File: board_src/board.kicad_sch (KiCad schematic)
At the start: 40 parts, among them J1 Conn_01x05, J16 Conn_01x05, J17 Conn_01x05, J18 Conn_02x20_Counter_Clockwise, J2 Conn_01x05, J20 Conn_02x20_Counter_Clockwise, J21 Conn_02x20_Counter_Clockwise, J22 Conn_02x20_Counter_Clockwise, J26 Conn_01x20_Socket, J27 Conn_01x20_Socket, J30 Conn_01x05, J31 Conn_01x05, J36 Conn_01x20_Socket, J37 Conn_01x20_Socket, J40 Conn_01x01_Pin, J41 Conn_01x01_Pin, J42 Conn_01x01_Pin, J43 Conn_01x01_Pin, J44 Conn_01x01_Pin, J46 Conn_01x01_Pin

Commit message: najnowsza wersja
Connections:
- no-connect marks 8 -> 2
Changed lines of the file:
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@@
-	)
-	(no_connect
-		(at 67.31 72.39)
-	)
-	(no_connect
-		(at 209.55 74.93)
-	)
-	(no_connect
-		(at 207.01 74.93)
 	)
 	(no_connect
@@
 	)
 	(no_connect
-		(at 69.85 72.39)
-	)
-	(no_connect
-		(at 204.47 74.93)
-	)
-	(no_connect
-		(at 64.77 72.39)
-	)
-	(no_connect

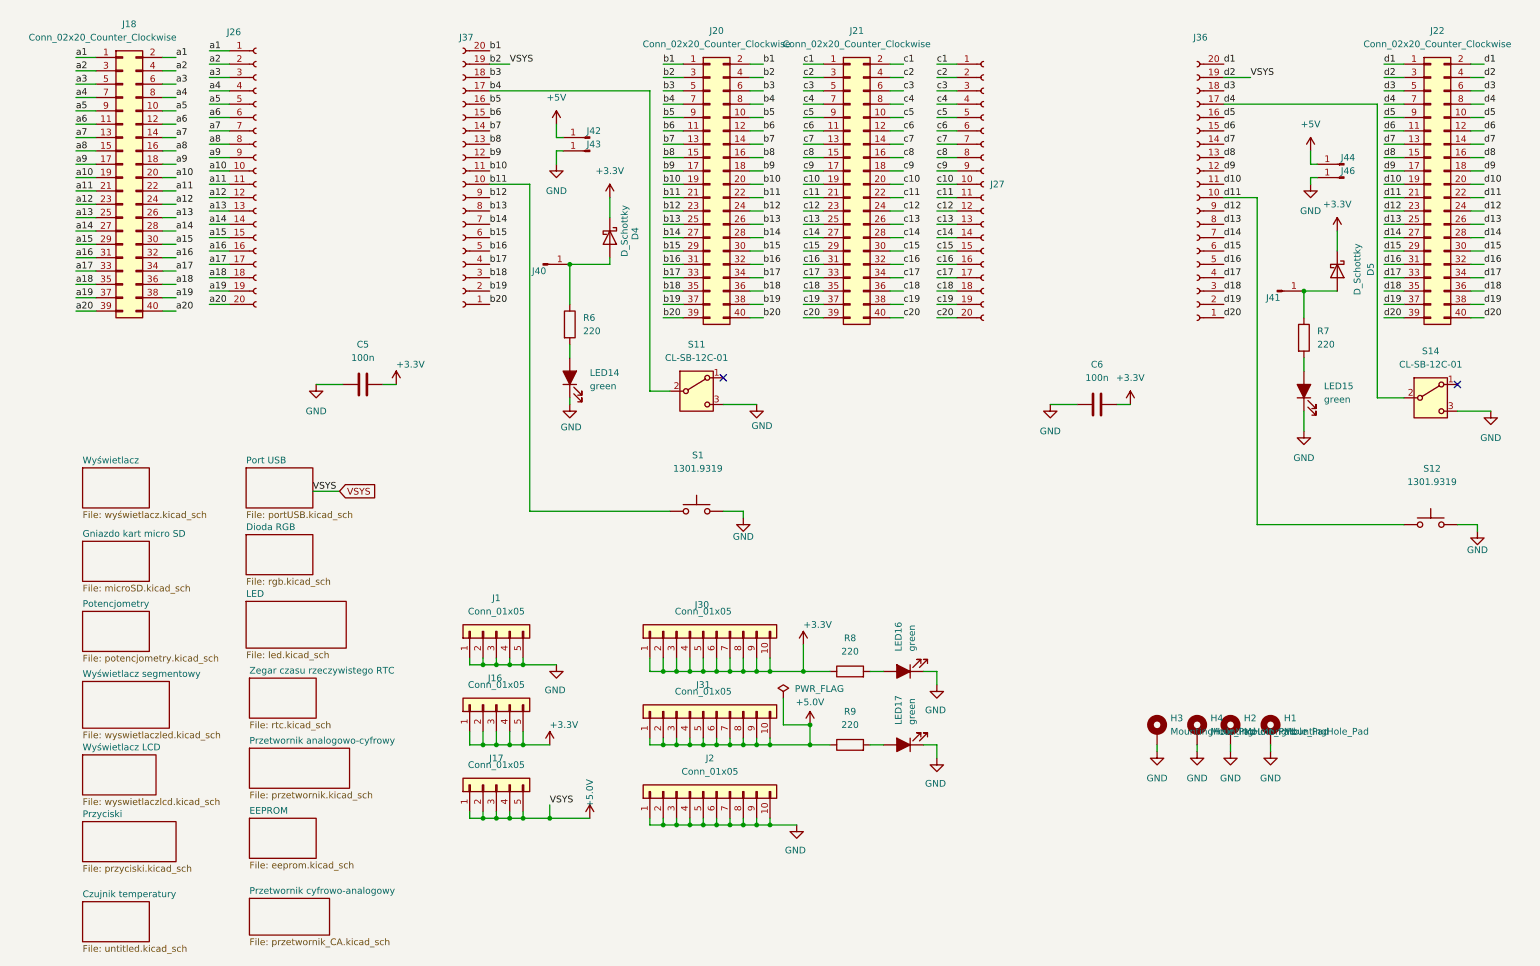
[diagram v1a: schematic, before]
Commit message: Poprawki w schematach. Rozpoczęte korekty płytki
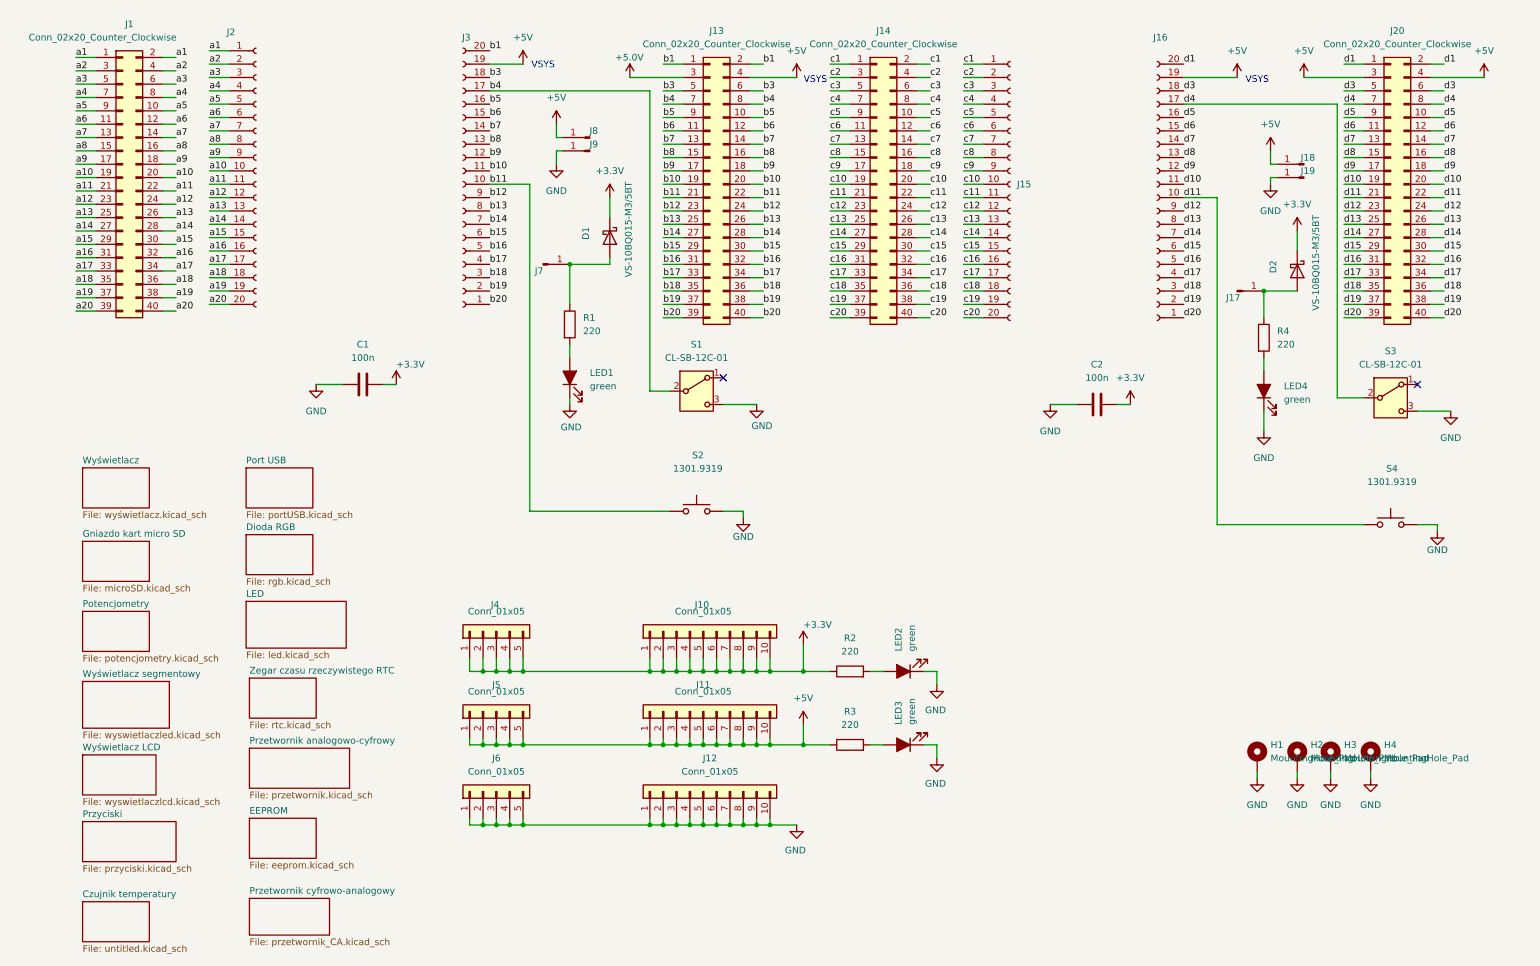
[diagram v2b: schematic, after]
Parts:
- removed D4, D5: D_Schottky, Diode_SMD:D_SMA, symbol Device:D_Schottky
- added D1, D2: VS-10BQ015-M3/5BT, Diode_SMD:D_SMB_Handsoldering, symbol Device:D_Schottky
- C1: renamed from C5; footprint Capacitor_SMD:C_0603_1608Metric -> Capacitor_SMD:C_0603_1608Metric_Pad1.08x0.95mm_HandSolder
- C2: renamed from C6; footprint Capacitor_SMD:C_0603_1608Metric -> Capacitor_SMD:C_0603_1608Metric_Pad1.08x0.95mm_HandSolder
- J1: renamed from J18; footprint Connector_PinHeader_2.54mm:PinHeader_2x20_P2.54mm_Vertical -> Connector_PinHeader_2.54mm:PinHeader_1x05_P2.54mm_Vertical
- J10: renamed from J30; footprint Connector_PinHeader_2.54mm:PinHeader_1x10_P2.54mm_Vertical -> Connector_PinHeader_2.54mm:PinHeader_2x02_P2.54mm_Vertical
- J11: renamed from J31; footprint Connector_PinHeader_2.54mm:PinHeader_1x10_P2.54mm_Vertical -> Connector_PinHeader_2.54mm:PinHeader_1x03_P2.54mm_Vertical
- J12: renamed from J2; footprint Connector_PinHeader_2.54mm:PinHeader_1x10_P2.54mm_Vertical -> footprints:112JTDARR01
- J13: renamed from J20; footprint Connector_PinHeader_2.54mm:PinHeader_2x20_P2.54mm_Vertical -> Connector_PinHeader_2.54mm:PinHeader_1x03_P2.54mm_Vertical
- J14: renamed from J21; footprint Connector_PinHeader_2.54mm:PinHeader_2x20_P2.54mm_Vertical -> Connector_PinHeader_2.54mm:PinHeader_1x07_P2.54mm_Vertical
- J15: renamed from J27; footprint Connector_PinSocket_2.54mm:PinSocket_1x20_P2.54mm_Vertical -> Connector_PinHeader_2.54mm:PinHeader_1x03_P2.54mm_Vertical
- J16: renamed from J36; footprint Connector_PinSocket_2.54mm:PinSocket_1x20_P2.54mm_Vertical -> Connector_PinHeader_2.54mm:PinHeader_1x05_P2.54mm_Vertical
- J17: renamed from J41; footprint Connector_PinHeader_2.54mm:PinHeader_1x01_P2.54mm_Vertical -> Connector_PinHeader_2.54mm:PinHeader_1x05_P2.54mm_Vertical
- J18: renamed from J44; footprint Connector_PinHeader_2.54mm:PinHeader_1x01_P2.54mm_Vertical -> Connector_PinHeader_2.54mm:PinHeader_2x20_P2.54mm_Vertical
- J19: renamed from J46; footprint Connector_PinHeader_2.54mm:PinHeader_1x01_P2.54mm_Vertical -> Connector_PinHeader_2.54mm:PinHeader_2x07_P2.54mm_Vertical
- J2: renamed from J26; footprint Connector_PinSocket_2.54mm:PinSocket_1x20_P2.54mm_Vertical -> Connector_PinHeader_2.54mm:PinHeader_1x10_P2.54mm_Vertical
- J3: renamed from J37; footprint Connector_PinSocket_2.54mm:PinSocket_1x20_P2.54mm_Vertical -> Connector_PinHeader_2.54mm:PinHeader_1x07_P2.54mm_Vertical
- J4: renamed from J16; footprint Connector_PinHeader_2.54mm:PinHeader_1x05_P2.54mm_Vertical -> Connector_PinHeader_2.54mm:PinHeader_1x04_P2.54mm_Vertical
- J5: renamed from J17; footprint Connector_PinHeader_2.54mm:PinHeader_1x05_P2.54mm_Vertical -> Connector_PinHeader_2.54mm:PinHeader_1x08_P2.54mm_Vertical
- J6: renamed from J1; footprint Connector_PinHeader_2.54mm:PinHeader_1x05_P2.54mm_Vertical -> Connector_PinHeader_2.54mm:PinHeader_1x02_P2.54mm_Vertical
- J7: renamed from J40; footprint Connector_PinHeader_2.54mm:PinHeader_1x01_P2.54mm_Vertical -> Connector_PinSocket_2.54mm:PinSocket_1x16_P2.54mm_Vertical
- J8: renamed from J42; footprint Connector_PinHeader_2.54mm:PinHeader_1x01_P2.54mm_Vertical -> Connector_PinHeader_2.54mm:PinHeader_1x04_P2.54mm_Vertical
- J9: renamed from J43; footprint Connector_PinHeader_2.54mm:PinHeader_1x01_P2.54mm_Vertical -> Connector_PinHeader_2.54mm:PinHeader_1x02_P2.54mm_Vertical
- LED1: renamed from LED14; footprint footprints:LEDC1608X100N -> footprints:ASMT-YTC7-0AA02
- LED2: renamed from LED16; footprint footprints:LEDC1608X100N -> LED_SMD:LED_0603_1608Metric_Pad1.05x0.95mm_HandSolder
- LED3: renamed from LED17; footprint footprints:LEDC1608X100N -> LED_SMD:LED_0603_1608Metric_Pad1.05x0.95mm_HandSolder
- LED4: renamed from LED15; footprint footprints:LEDC1608X100N -> LED_SMD:LED_0603_1608Metric_Pad1.05x0.95mm_HandSolder
- R1: renamed from R6; footprint Resistor_SMD:R_0603_1608Metric -> Resistor_SMD:R_0603_1608Metric_Pad0.98x0.95mm_HandSolder
- R2: renamed from R8; footprint Resistor_SMD:R_0603_1608Metric -> Resistor_SMD:R_0603_1608Metric_Pad0.98x0.95mm_HandSolder
- R3: renamed from R9; footprint Resistor_SMD:R_0603_1608Metric -> Resistor_SMD:R_0603_1608Metric_Pad0.98x0.95mm_HandSolder
- R4: renamed from R7; footprint Resistor_SMD:R_0603_1608Metric -> Resistor_SMD:R_0603_1608Metric_Pad0.98x0.95mm_HandSolder
- S1: renamed from S11; footprint footprints:JS102011CQN -> Button_Switch_THT:SW_PUSH_6mm_H9.5mm
- S3: renamed from S14; footprint footprints:JS102011CQN -> Button_Switch_THT:SW_PUSH_6mm_H9.5mm
- renumbered H3 to H1, H4 to H2, H2 to H3, H1 to H4, J22 to J20, S1 to S2, S12 to S4
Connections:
- net +3.3V: now also D1.1 (K), D2.1 (K)
- net +5.0V: no longer J11.1 (Pin_1), J11.10 (Pin_10), J11.2 (Pin_2), J11.3 (Pin_3), J11.4 (Pin_4), J11.5 (Pin_5), J11.6 (Pin_6), J11.7 (Pin_7), J11.8 (Pin_8), J11.9 (Pin_9), J13.4 (Pin_4), J16.19 (Pin_19), J20.3 (Pin_3), J20.4 (Pin_4), J3.19 (Pin_19), J5.1 (Pin_1), J5.2 (Pin_2), J5.3 (Pin_3), J5.4 (Pin_4), J5.5 (Pin_5), R3.1
- net +5V: now also J11.1 (Pin_1), J11.10 (Pin_10), J11.2 (Pin_2), J11.3 (Pin_3), J11.4 (Pin_4), J11.5 (Pin_5), J11.6 (Pin_6), J11.7 (Pin_7), J11.8 (Pin_8), J11.9 (Pin_9), J13.4 (Pin_4), J16.19 (Pin_19), J20.3 (Pin_3), J20.4 (Pin_4), J3.19 (Pin_19), J5.1 (Pin_1), J5.2 (Pin_2), J5.3 (Pin_3), J5.4 (Pin_4), J5.5 (Pin_5), R3.1
- net at J7.1 (Pin_1), R1.1: now also D1.2 (A)
- net at J17.1 (Pin_1), R4.1: now also D2.2 (A)
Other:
- note added: "VSYS"
- moved on the sheet: H1, H2, H3, H4, J14, J15, J16, J17, J18, J19, J20, J4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

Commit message: Naniesione poprawki na projekcie płytki. Wersja końcowa
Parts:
- R3: value 220 -> 470
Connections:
- net a13 is gone; now on net GND: J1.25 (Pin_25), J1.26 (Pin_26), J2.13 (Pin_13)
- net a18 is gone; now on net GND: J1.35 (Pin_35), J1.36 (Pin_36), J2.18 (Pin_18)
- net a3 is gone; now on net GND: J1.5 (Pin_5), J1.6 (Pin_6), J2.3 (Pin_3)
- net a8 is gone; now on net GND: J1.15 (Pin_15), J1.16 (Pin_16), J2.8 (Pin_8)
- net b13 is gone; now on net GND: J13.25 (Pin_25), J13.26 (Pin_26), J3.8 (Pin_8)
- net b18 is gone; now on net GND: J13.35 (Pin_35), J13.36 (Pin_36), J3.3 (Pin_3)
- net b3 is gone; now on net GND: J13.5 (Pin_5), J13.6 (Pin_6), J3.18 (Pin_18)
- net b8 is gone; now on net GND: J13.15 (Pin_15), J13.16 (Pin_16), J3.13 (Pin_13)
- net c13 is gone; now on net GND: J14.25 (Pin_25), J14.26 (Pin_26), J15.13 (Pin_13)
- net c18 is gone; now on net GND: J14.35 (Pin_35), J14.36 (Pin_36), J15.18 (Pin_18)
- net c3 is gone; now on net GND: J14.5 (Pin_5), J14.6 (Pin_6), J15.3 (Pin_3)
- net c8 is gone; now on net GND: J14.15 (Pin_15), J14.16 (Pin_16), J15.8 (Pin_8)
- net d13 is gone; now on net GND: J16.8 (Pin_8), J20.25 (Pin_25), J20.26 (Pin_26)
- net d18 is gone; now on net GND: J16.3 (Pin_3), J20.35 (Pin_35), J20.36 (Pin_36)
- net d3 is gone; now on net GND: J16.18 (Pin_18), J20.5 (Pin_5), J20.6 (Pin_6)
- net d8 is gone; now on net GND: J16.13 (Pin_13), J20.15 (Pin_15), J20.16 (Pin_16)
- net +5V: no longer J13.4 (Pin_4), J16.19 (Pin_19), J20.3 (Pin_3), J20.4 (Pin_4), J3.19 (Pin_19)
- net +5.0V renamed VSYS
- net VSYS: now also J13.4 (Pin_4), J3.19 (Pin_19)
- new net VSYS_2: J16.19 (Pin_19), J20.3 (Pin_3), J20.4 (Pin_4)
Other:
- note added: "3V3_EN"
- note added: "Moduł Raspberry Pi Pico"
- note added: "RESET"
- note removed: "VSYS"
- moved on the sheet: C2, D1, D2, J1, J13, J14, J15, J16, J17, J18, J19, J2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
